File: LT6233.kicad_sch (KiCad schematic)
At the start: 15 parts, among them U3001 LT6233CS6#TRMPBF, U3002 PBSS4230T,215

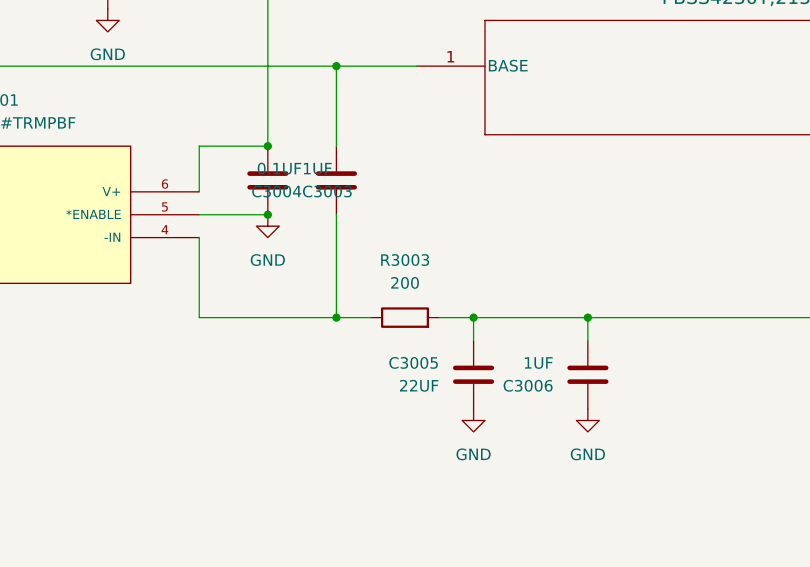
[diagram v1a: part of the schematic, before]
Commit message: Schematic Changes
Added Manufacturer/MPN/Description Fields to parts
Added libraries to project
Modified FMC schematic to use new symbol
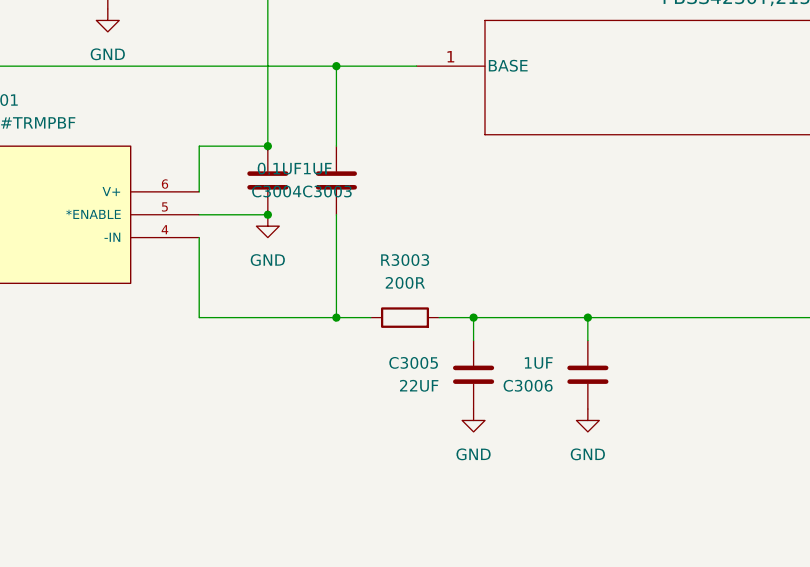
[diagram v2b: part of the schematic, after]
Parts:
- C3001, C3005: Manufacturer (none) -> Panasonic; Manufacturer Part Number (none) -> EEF-CD1B220R
- C3002, C3008: Manufacturer (none) -> Murata; Manufacturer Part Number (none) -> GRM31CR61A476ME15L
- C3003, C3006, C3007: Manufacturer (none) -> Murata; Manufacturer Part Number (none) -> GRM188R61E105KA12D
- C3004: Manufacturer (none) -> Murata; Manufacturer Part Number (none) -> GRM155R61A104KA01D
- FB3001, FB3002: Manufacturer (none) -> Würth; Manufacturer Part Number (none) -> 742792040
- R3001: Manufacturer (none) -> YAGEO; Manufacturer Part Number (none) -> RC0603FR-074K42L
- R3002: Manufacturer (none) -> YAGEO; Manufacturer Part Number (none) -> RC0603FR-0711K5L
- R3003: value 200 -> 200R; Manufacturer (none) -> Susumu; Manufacturer Part Number (none) -> RR0816P-201-D
- U3001: Manufacturer (none) -> Analog Devices; Manufacturer Part Number (none) -> LT6233CS6#TRMPBF
- U3002: Manufacturer (none) -> Nexperia; Manufacturer Part Number (none) -> PBSS4230T,215

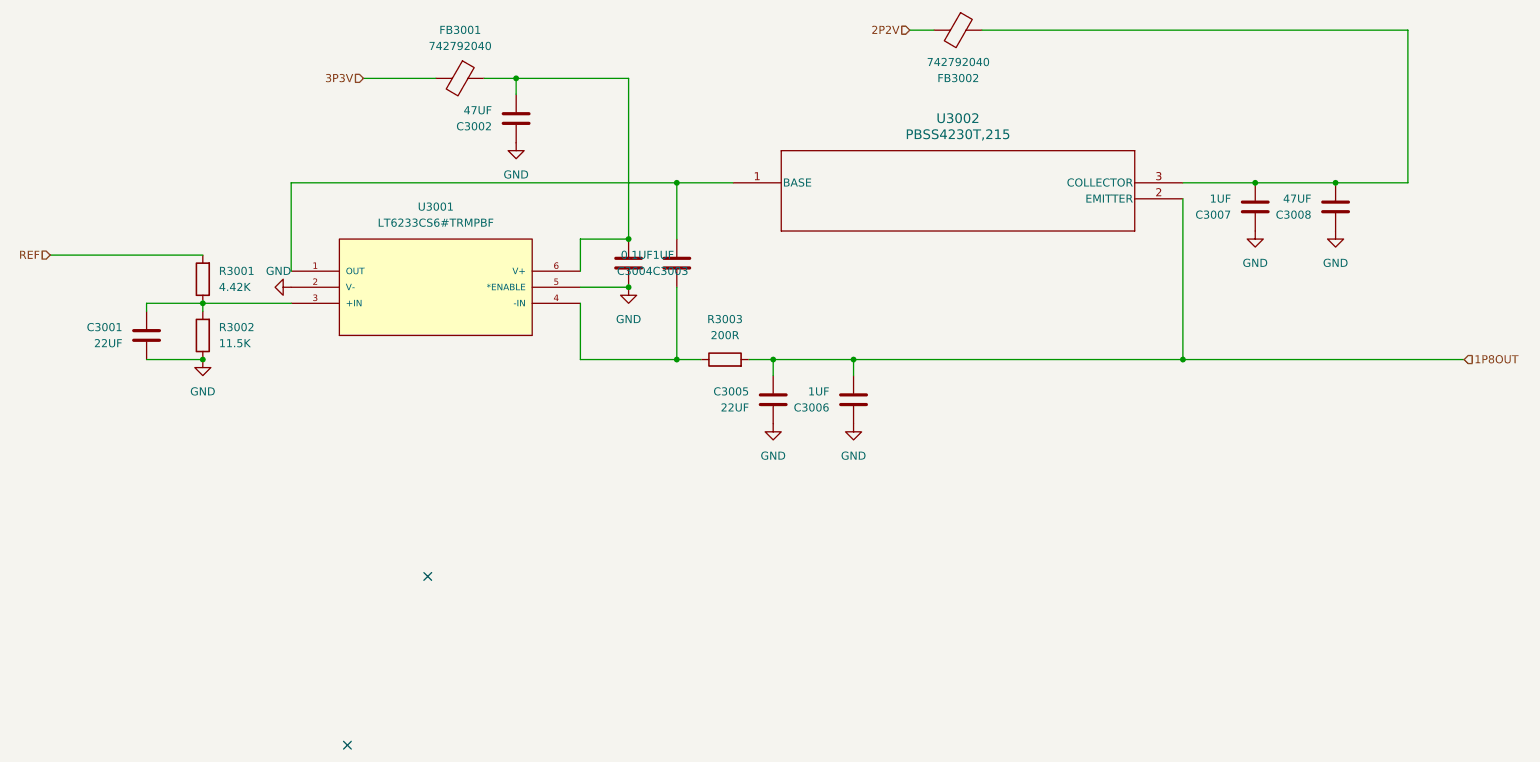
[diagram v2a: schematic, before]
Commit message: Schematics update
Cleaned up RF ADC and front end sections.
Verified that changes did not changes anything about the layout.
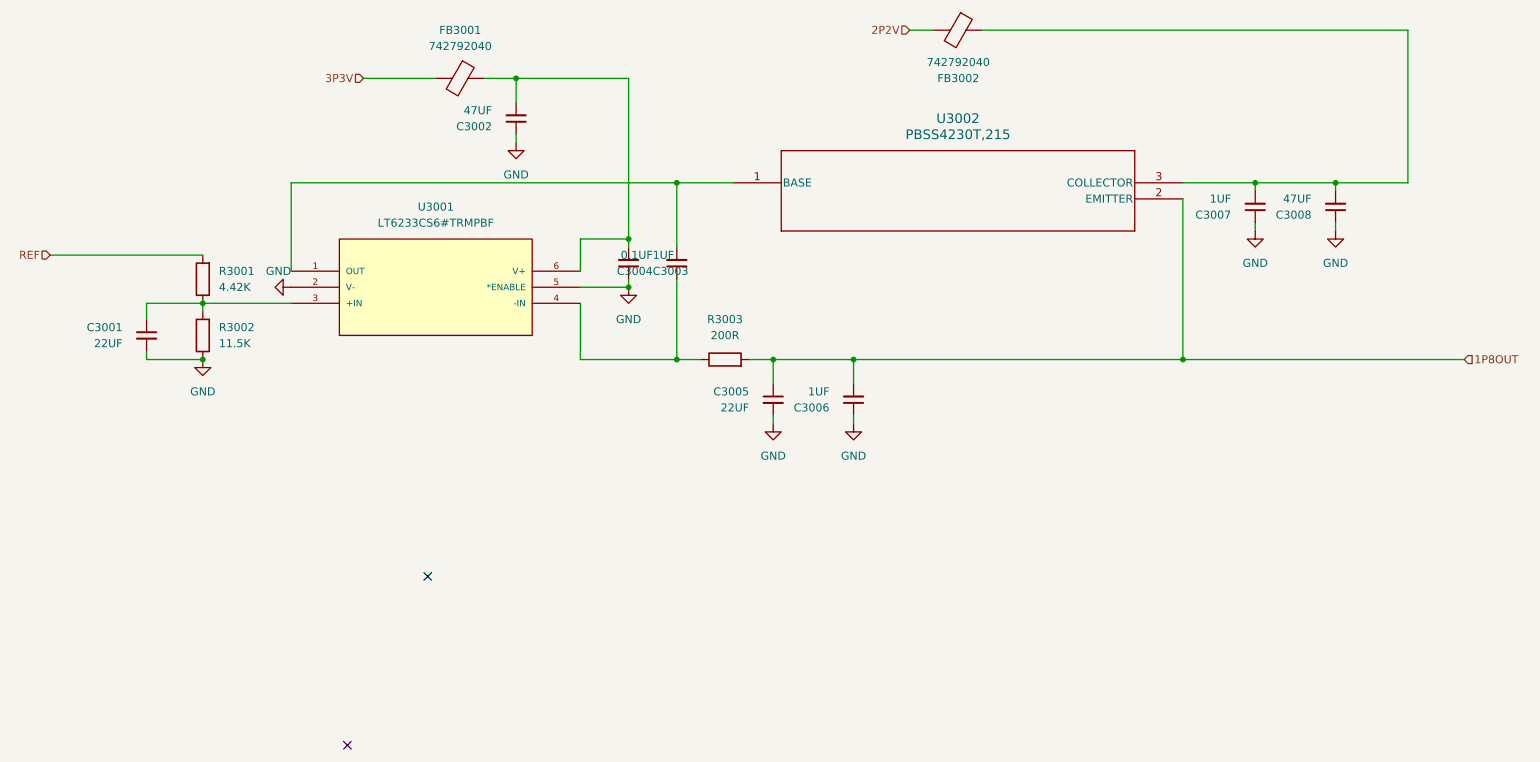
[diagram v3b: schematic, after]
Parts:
- C3001, C3002, C3003, C3004, C3005, C3006, C3007, C3008: symbol Device:C -> Device:C_Small

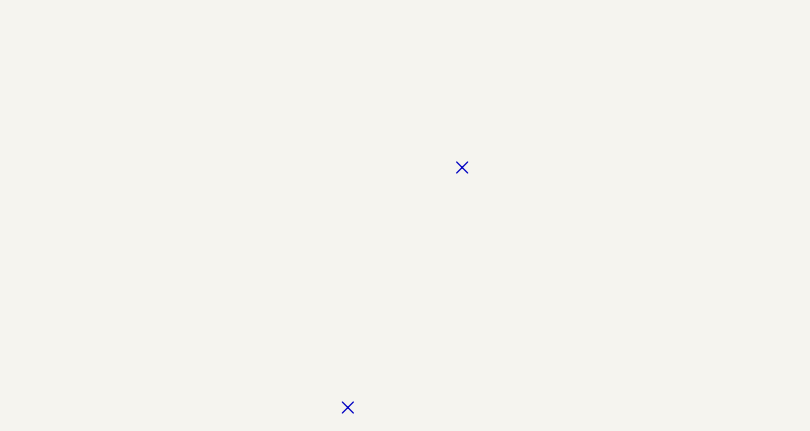
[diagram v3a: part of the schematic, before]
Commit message: Updated some Schematics
- updated slowmon schematic
- updated diff to se schematic
- cleaned up DRC/ERC errors
No changes were made that effected the PCB layout
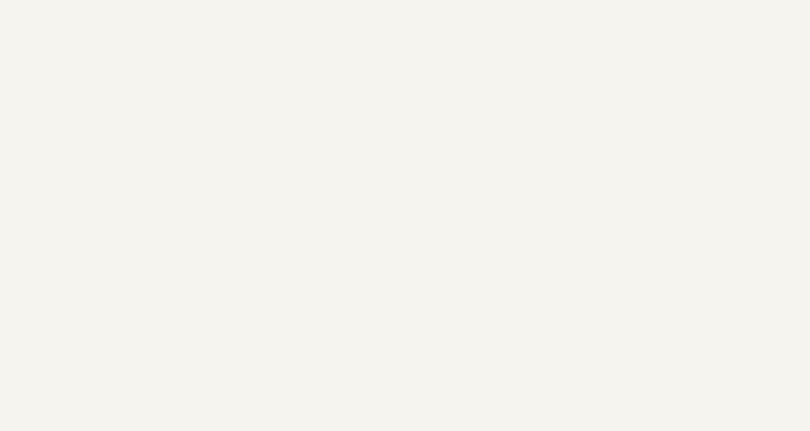
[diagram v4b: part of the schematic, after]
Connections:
- no-connect marks 2 -> 0
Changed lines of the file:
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@@
 		(color 0 0 0 0)
-	)
-	(no_connect
-		(at 76.2 173.99)
-	)
-	(no_connect
-		(at 88.9 147.32)
 	)
 	(wire

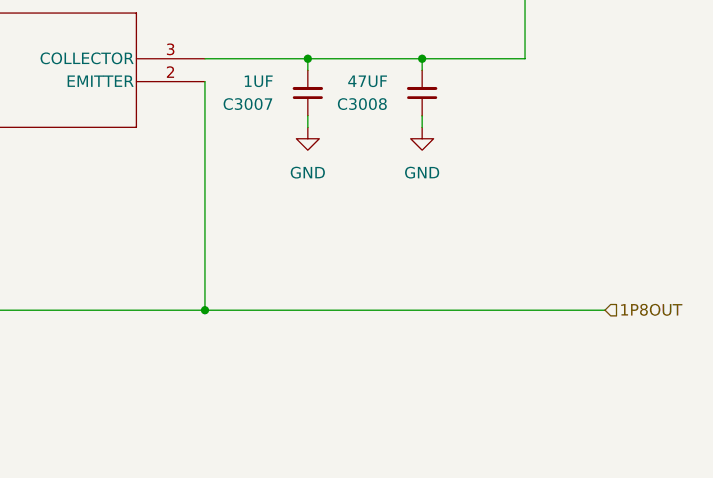
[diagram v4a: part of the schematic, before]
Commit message: resolve duplicate power flag
kicad 8 complains about two power flags on VSS1P8V net,
one each on ADC0 and ADC1 pages.  Consolidate to one
flag on the U35_LT6233 page.
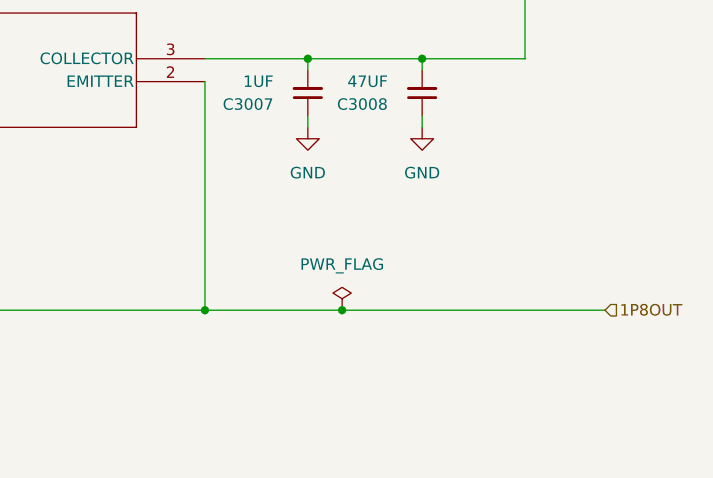
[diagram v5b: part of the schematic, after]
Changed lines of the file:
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@@
+	)
+	(junction
+		(at 223.52 113.03)
+		(diameter 0)
+		(color 0 0 0 0)
 	)
 	(junction
@@
 	(wire
 		(pts
+			(xy 223.52 113.03) (xy 252.73 113.03)
+		)
+		(stroke
+			(width 0)
+			(type default)
+		)
+	)
+	(wire
+		(pts
 			(xy 219.71 85.09) (xy 232.41 85.09)
 		)
@@
 	(wire
 		(pts
-			(xy 208.28 113.03) (xy 252.73 113.03)
+			(xy 208.28 113.03) (xy 223.52 113.03)
 		)
 		(stroke
@@
 		)
 	)
+	(symbol
+		(lib_id "power:PWR_FLAG")
+		(at 223.52 113.03 0)
+		(unit 1)
+		(exclude_from_sim no)
+		(in_bom yes)
+		(on_board yes)
+		(dnp no)
+		(fields_autoplaced yes)
+		(property "Reference" "#FLG04"
+			(at 223.52 111.125 0)
+			(effects
+				(font
+					(size 1.27 1.27)
+				)
+				(hide yes)
+			)
+		)
+		(property "Value" "PWR_FLAG"
+			(at 223.52 107.95 0)
+			(effects
+				(font
+					(size 1.27 1.27)
+				)
+			)
+		)
+		(property "Footprint" ""
+			(at 223.52 113.03 0)
+			(effects
+				(font
+					(size 1.27 1.27)
+				)
+				(hide yes)
+			)
+		)
+		(property "Datasheet" "~"
+			(at 223.52 113.03 0)
+			(effects
+				(font
+					(size 1.27 1.27)
+				)
+				(hide yes)
+			)
+		)
+		(property "Description" "Special symbol for telling ERC where power comes from"
+			(at 223.52 113.03 0)
+			(effects
+				(font
+					(size 1.27 1.27)
+				)
+				(hide yes)
+			)
+		)
+		(pin "1"
+		)
+		(instances
+			(project ""
+				(path "/00000000-0000-0000-0000-000000000003/00000000-0000-0000-0000-000000000002/84286640-adb6-4b0c-9fb1-cd512b643b0c"
+					(reference "#FLG04")
+					(unit 1)
+				)
+			)
+		)
+	)
